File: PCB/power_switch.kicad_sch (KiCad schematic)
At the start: 5 parts, among them U4 TPS2001CDGNR

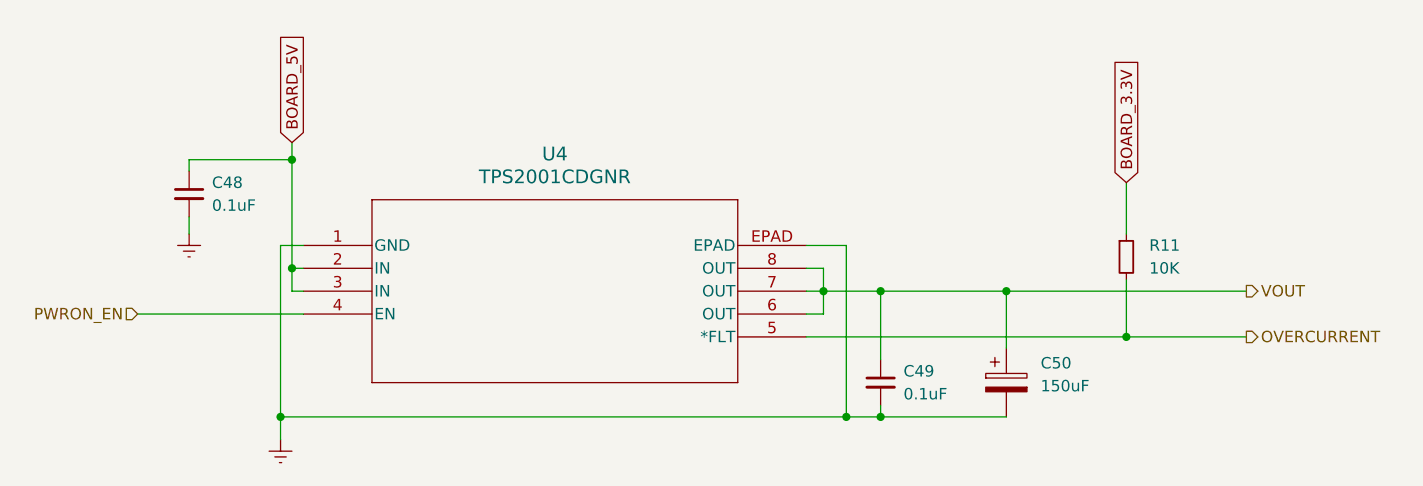
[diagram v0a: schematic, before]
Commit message: comply with ERC
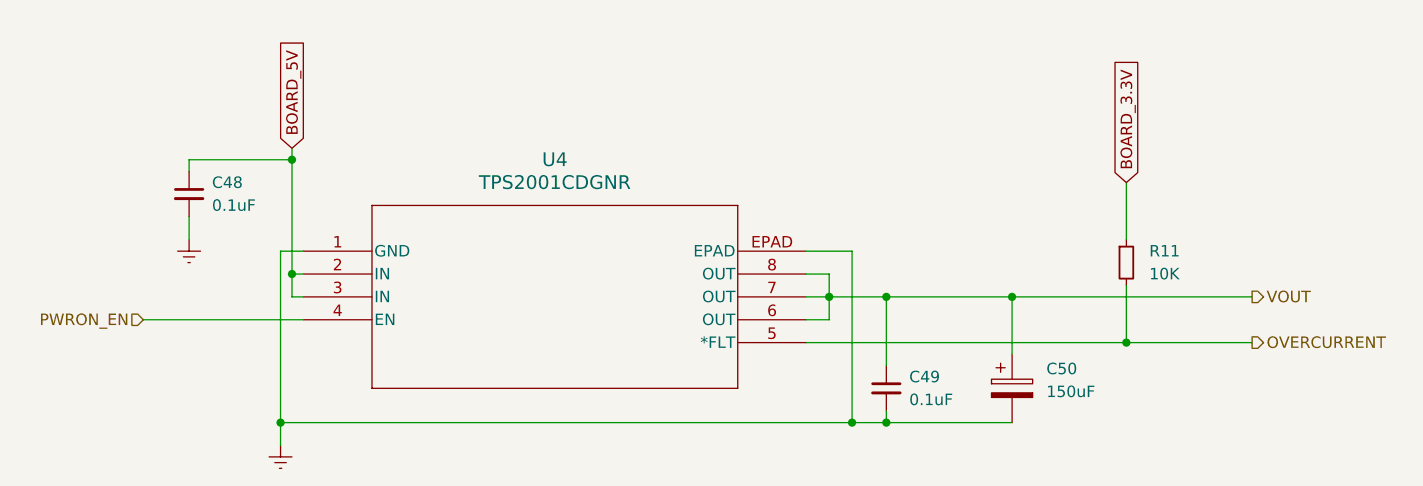
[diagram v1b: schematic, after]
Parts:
- U4: footprint DGN8_1P89X1P57 -> my_global:DGN8_1P89X1P57; symbol MyLibrary:TPS2001CDGNR -> my_global:TPS2001CDGNR
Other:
- moved on the sheet: C49, C50, R11, U4

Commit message: adjust schematic to match real components, assign footprints
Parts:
- C48, C49: footprint (none) -> Capacitor_SMD:C_0402_1005Metric
- C50: footprint (none) -> Capacitor_Tantalum_SMD:CP_EIA-7343-15_Kemet-W
- R11: footprint (none) -> Resistor_SMD:R_0402_1005Metric
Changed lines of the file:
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@@
 			)
 		)
-		(property "Footprint" ""
+		(property "Footprint" "Capacitor_SMD:C_0402_1005Metric"
 			(at 123.19 78.74 0)
 			(effects
@@
 			)
 		)
-		(property "Footprint" ""
+		(property "Footprint" "Resistor_SMD:R_0402_1005Metric"
 			(at 149.86 64.77 0)
 			(effects
@@
 			)
 		)
-		(property "Footprint" ""
+		(property "Footprint" "Capacitor_Tantalum_SMD:CP_EIA-7343-15_Kemet-W"
 			(at 138.1252 82.55 0)
 			(effects
@@
 			)
 		)
-		(property "Footprint" ""
+		(property "Footprint" "Capacitor_SMD:C_0402_1005Metric"
 			(at 45.72 57.15 0)
 			(effects

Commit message: pcb v1.2 with JLC mappings
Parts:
- C50: footprint Capacitor_Tantalum_SMD:CP_EIA-7343-15_Kemet-W -> my_global:CAP_EEFCX0J151XR
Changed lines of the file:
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@@
 			)
 		)
-		(property "Footprint" "Capacitor_Tantalum_SMD:CP_EIA-7343-15_Kemet-W"
+		(property "Footprint" "my_global:CAP_EEFCX0J151XR"
 			(at 138.1252 82.55 0)
 			(effects
